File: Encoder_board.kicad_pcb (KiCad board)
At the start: 2 copper layers, 70 x 70 mm, 77 parts, among them J1 Conn_01x05_Socket_RS485, J2 CAN_OUT, J3 Conn_01x05_Socket_Encoder4, J4 Conn_01x05_Socket_Encoder1, J5 Conn_01x05_Socket_Encoder2, J6 Conn_01x05_Socket_Encoder5, J7 ST-Link_pinsocket, J8 Conn_01x05_Socket_Encoder3, SW1 SW_Boot, SW2 SW_Reset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

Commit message: シルクを一部修正
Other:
- board text added: "En_5_Tim8"
- board text removed: "En_5_Iim8"
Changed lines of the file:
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@@
 	)
 	(gr_text "JLCJLCJLCJLC"
-		(at 151.4 122.4 0)
+		(at 158.8 112.9 90)
 		(layer "F.SilkS")
 		(effects
@@
 		)
 	)
-	(gr_text "En_5_Iim8"
+	(gr_text "En_5_Tim8"
 		(at 118.4 80.8 90)
 		(layer "F.SilkS" knockout)

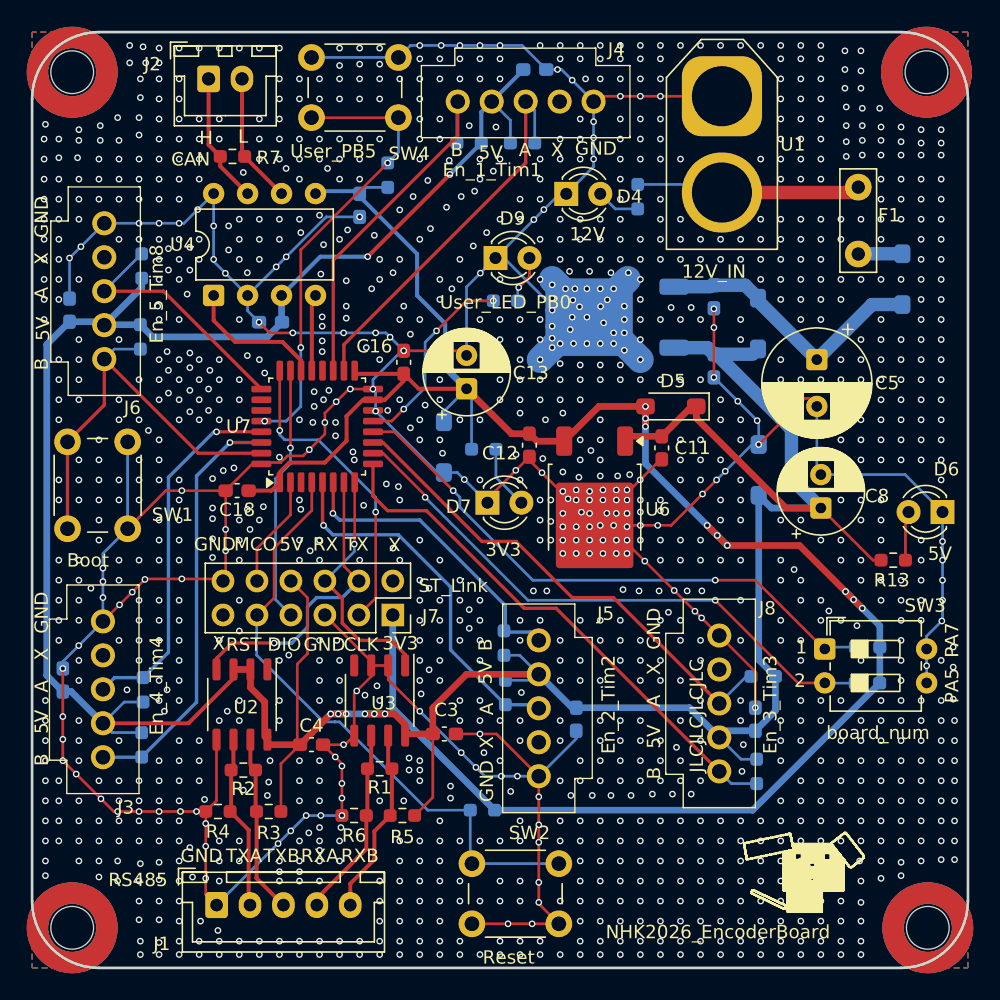
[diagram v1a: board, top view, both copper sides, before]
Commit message: 基板外形を修正
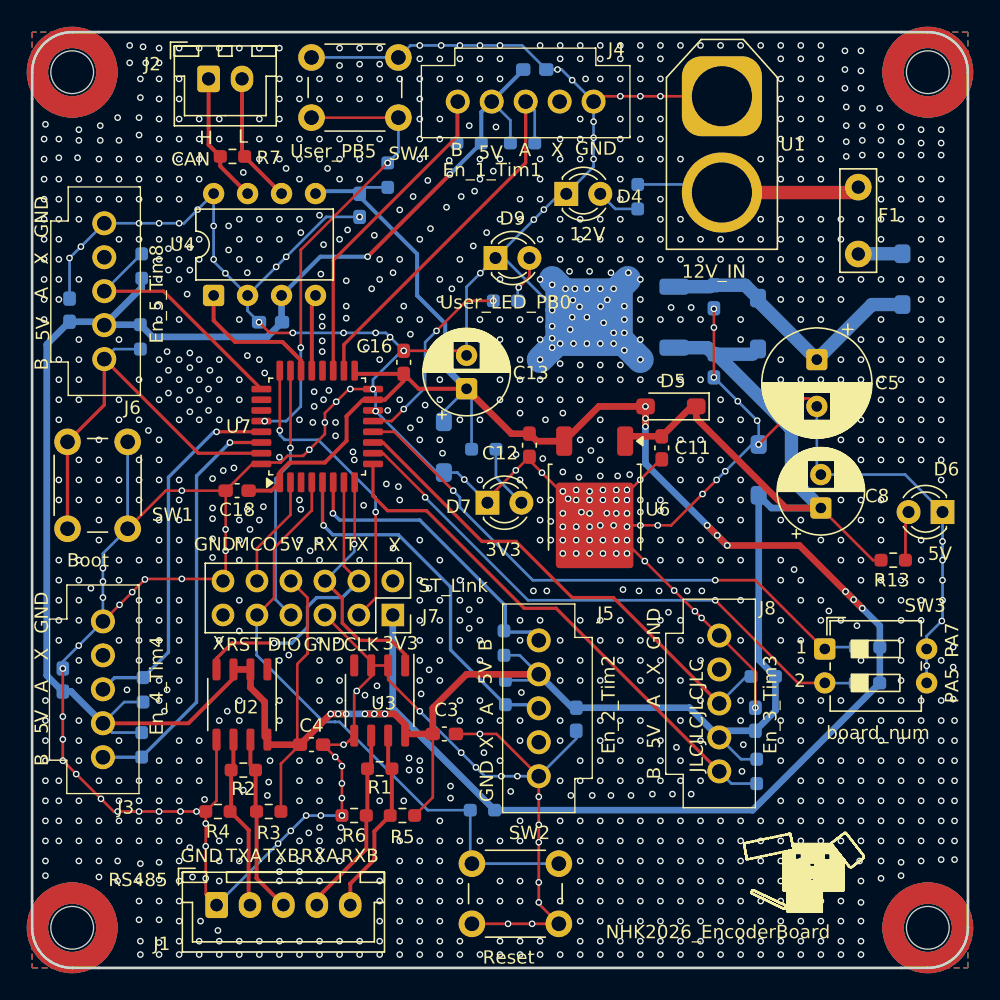
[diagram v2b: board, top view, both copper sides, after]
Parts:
- moved REF** 0.10 mm to (175.5, 60.5)
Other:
- outline, holes or cut-outs redrawn
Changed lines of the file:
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@@
 			(outputformat 1)
 			(mirror no)
-			(drillshape 1)
+			(drillshape 0)
 			(scaleselection 1)
-			(outputdirectory "")
+			(outputdirectory "./")
 		)
 	)
@@
 	(footprint "MountingHole:MountingHole_3.2mm_M3"
 		(layer "F.Cu")
-		(at 175.4 60.5)
+		(at 175.5 60.5)
 		(descr "Mounting Hole 3.2mm, M3, no annular, generated by kicad-footprint-generator mountinghole.py")
 		(tags "mountinghole M3")
@@
 	)
 	(gr_circle
-		(center 175.4 60.5)
-		(end 175.4 63.1)
+		(center 175.5 60.5)
+		(end 175.5 63.1)
 		(stroke
 			(width 1.6)
@@
 	)
 	(gr_circle
-		(center 175.4 60.5)
-		(end 175.4 63.1)
+		(center 175.5 60.5)
+		(end 175.5 63.1)
 		(stroke
 			(width 1.6)
@@
 	)
 	(gr_line
+		(start 108.5 124.51833)
+		(end 108.5 122.5)
+		(stroke
+			(width 0.2)
+			(type solid)
+		)
+		(layer "Edge.Cuts")
+	)
+	(gr_arc
+		(start 111.518477 127.5)
+		(mid 109.391745 126.634386)
+		(end 108.5 124.518477)
+		(stroke
+			(width 0.2)
+			(type solid)
+		)
+		(layer "Edge.Cuts")
+	)
+	(gr_arc
+		(start 178.5 124.5)
+		(mid 177.62132 126.62132)
+		(end 175.5 127.5)
+		(stroke
+			(width 0.2)
+			(type solid)
+		)
+		(layer "Edge.Cuts")
+	)
+	(gr_line
 		(start 113.5 57.5)
 		(end 173.5 57.5)
@@
 		(layer "Edge.Cuts")
 	)
-	(gr_arc
-		(start 173.5 57.5)
-		(mid 177.035534 58.964466)
-		(end 178.5 62.5)
+	(gr_line
+		(start 178.503998 122.5)
+		(end 178.503998 124.5)
 		(stroke
 			(width 0.2)
@@
 		(layer "Edge.Cuts")
 	)
-	(gr_arc
+	(gr_line
+		(start 108.5 60.5)
+		(end 108.5 62.5)
+		(stroke
+			(width 0.2)
+			(type solid)
+		)
+		(layer "Edge.Cuts")
+	)
+	(gr_line
 		(start 113.5 127.5)
-		(mid 109.964466 126.035534)
-		(end 108.5 122.5)
+		(end 111.518477 127.5)
 		(stroke
 			(width 0.2)
@@
 	)
 	(gr_arc
-		(start 108.5 62.5)
-		(mid 109.964466 58.964466)
-		(end 113.5 57.5)
+		(start 175.5 57.5)
+		(mid 177.62132 58.37868)
+		(end 178.5 60.5)
 		(stroke
 			(width 0.2)
@@
 	)
 	(gr_arc
-		(start 178.5 122.5)
-		(mid 177.035534 126.035534)
+		(start 108.5 60.5)
+		(mid 109.37868 58.37868)
+		(end 111.5 57.5)
+		(stroke
+			(width 0.2)
+			(type solid)
+		)
+		(layer "Edge.Cuts")
+	)
+	(gr_line
+		(start 175.5 57.5)
+		(end 173.5 57.5)
+		(stroke
+			(width 0.2)
+			(type solid)
+		)
+		(layer "Edge.Cuts")
+	)
+	(gr_line
+		(start 175.5 127.5)
 		(end 173.5 127.5)
 		(stroke
@@
 	)
 	(gr_line
+		(start 178.5 60.5)
+		(end 178.503998 62.5)
+		(stroke
+			(width 0.2)
+			(type solid)
+		)
+		(layer "Edge.Cuts")
+	)
+	(gr_line
+		(start 111.5 57.5)
+		(end 113.5 57.5)
+		(stroke
+			(width 0.2)
+			(type solid)
+		)
+		(layer "Edge.Cuts")
+	)
+	(gr_line
 		(start 173.5 127.5)
 		(end 113.5 127.5)
@@
 	)
 	(gr_rect
-		(start 175.4 57.5)
-		(end 178.4 60.5)
+		(start 175.5 57.5)
+		(end 178.5 60.5)
 		(stroke
 			(width 0.1)
